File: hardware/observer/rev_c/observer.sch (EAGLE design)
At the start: 61 parts, among them J1 CON_HEADER_2X05-SMD+SHROUDED, J2 CON_HEADER_2X05-SMD+SHROUDED, J3 TC2030-CC2538-BL-NL, J4 JUMPER-PTH-2-NO, J5 PINHD-2X8/SMD, J6 CON_HEADER_2X05-PTH+SHROUDED_A, P9/P8 BBB_HEADER, U1 LPS331AP, U10 TPS62740, U11 DMG1013UW-7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

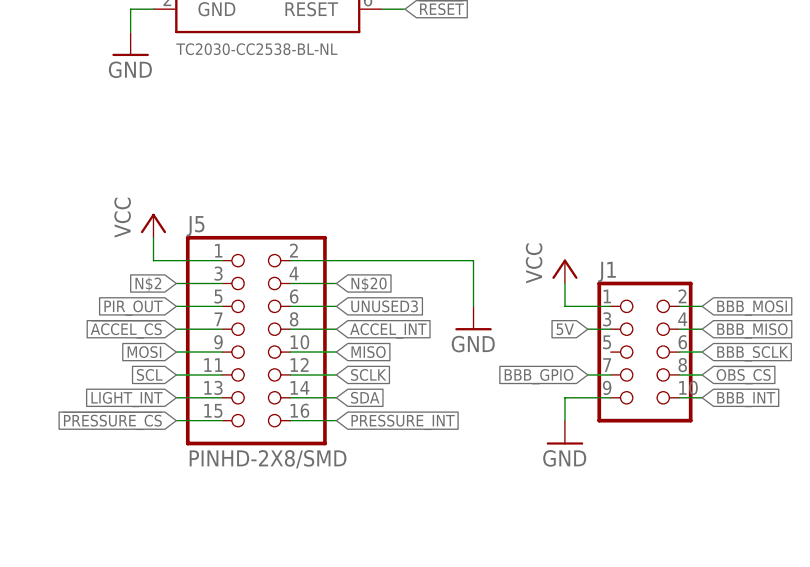
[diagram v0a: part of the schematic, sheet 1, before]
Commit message: connected opamp gate signal to header for debugging
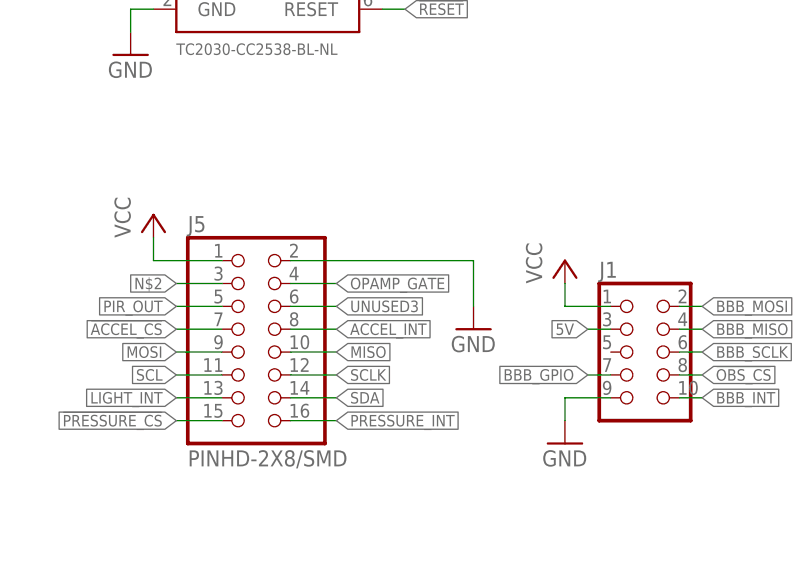
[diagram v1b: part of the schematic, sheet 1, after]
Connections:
- removed net N$20: J5.4
- net OPAMP_GATE: now also J5.4
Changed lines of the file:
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@@
-</segment>
-</net>
-<net name="N$20" class="0">
-<segment>
-<pinref part="J5" gate="G$1" pin="4"/>
-<wire x1="35.56" y1="30.48" x2="30.48" y2="30.48" width="0.1524" layer="91"/>
-<label x="35.56" y="30.48" size="1.27" layer="95" xref="yes"/>
 </segment>
 </net>
@@
 <label x="38.1" y="78.74" size="1.4224" layer="95" xref="yes"/>
 </segment>
+<segment>
+<pinref part="J5" gate="G$1" pin="4"/>
+<wire x1="35.56" y1="30.48" x2="30.48" y2="30.48" width="0.1524" layer="91"/>
+<label x="35.56" y="30.48" size="1.27" layer="95" xref="yes"/>
+</segment>
 </net>
